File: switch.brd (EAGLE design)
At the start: 11.6 x 31.7 mm, 3 parts

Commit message: updated
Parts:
- U$1: value MICROBIT_PAD -> pin1
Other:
- board size 11.6 x 31.7 mm -> 11.6 x 37.7 mm
- board text added: "PinwheelRobotics"
- board text added: "care@pinwheel"
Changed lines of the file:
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@@
 <setting verticaltext="up"/>
 </settings>
-<grid distance="50" unitdist="mil" unit="mm" style="lines" multiple="1" display="yes" altdistance="5" altunitdist="mil" altunit="mm"/>
+<grid distance="0.5" unitdist="mm" unit="mm" style="lines" multiple="1" display="yes" altdistance="5" altunitdist="mil" altunit="mm"/>
 <layers>
 <layer number="1" name="Top" color="4" fill="1" visible="yes" active="yes"/>
@@
 <layer number="43" name="vRestrict" color="2" fill="10" visible="yes" active="yes"/>
 <layer number="44" name="Drills" color="7" fill="1" visible="no" active="yes"/>
-<layer number="45" name="Holes" color="7" fill="1" visible="no" active="yes"/>
+<layer number="45" name="Holes" color="7" fill="1" visible="yes" active="yes"/>
 <layer number="46" name="Milling" color="3" fill="1" visible="no" active="yes"/>
 <layer number="47" name="Measures" color="7" fill="1" visible="no" active="yes"/>
@@
 <board>
 <plain>
-<wire x1="13.97" y1="11.43" x2="25.578" y2="11.43" width="0" layer="20"/>
-<wire x1="25.578" y1="11.43" x2="25.578" y2="43.17" width="0" layer="20"/>
-<wire x1="25.578" y1="43.17" x2="13.97" y2="43.17" width="0" layer="20"/>
-<wire x1="13.97" y1="43.17" x2="13.97" y2="11.43" width="0" layer="20"/>
+<wire x1="13.97" y1="45.206540625" x2="13.97" y2="10.297284375" width="0" layer="20"/>
+<wire x1="13.97" y1="10.297284375" x2="15.837284375" y2="8.43" width="0" layer="20" curve="90"/>
+<wire x1="15.837284375" y1="8.43" x2="23.637571875" y2="8.43" width="0" layer="20"/>
+<wire x1="23.637571875" y1="8.43" x2="25.578" y2="10.370428125" width="0" layer="20" curve="90"/>
+<wire x1="25.578" y1="10.370428125" x2="25.578" y2="45.098121875" width="0" layer="20"/>
+<wire x1="25.578" y1="45.098121875" x2="24.506121875" y2="46.17" width="0" layer="20" curve="90"/>
+<wire x1="24.506121875" y1="46.17" x2="14.933459375" y2="46.17" width="0" layer="20"/>
+<wire x1="14.933459375" y1="46.17" x2="13.97" y2="45.206540625" width="0" layer="20" curve="90"/>
+<hole x="16.004" y="10.574" drill="3"/>
+<hole x="23.498" y="10.574" drill="3"/>
+<hole x="16.004" y="43.884" drill="3"/>
+<hole x="23.496" y="44.006" drill="3"/>
+<text x="16.121" y="18.613" size="1.4224" layer="21" rot="R90">PinwheelRobotics</text>
+<text x="25.35" y="33.449" size="1.4224" layer="22" rot="MR270">care@pinwheel</text>
 </plain>
 <attributes>
@@
 <attribute name="SF_SKU" value="COM-00097" x="-1.27" y="62.865" size="1.778" layer="27" rot="R180" display="off"/>
 </element>
-<element name="U$1" library="microbit" package="MICROBIT_PAD" value="MICROBIT_PAD" x="20.066" y="15.748" smashed="yes" rot="R180">
-<attribute name="NAME" x="15.24" y="21.59" size="1.27" layer="21" rot="R270"/>
-</element>
-<element name="U$2" library="microbit" package="MICROBIT_PAD" value="MICROBIT_PAD" x="20.193" y="38.862" smashed="yes">
-<attribute name="NAME" x="16.129" y="36.703" size="1.27" layer="21" rot="R90"/>
-</element>
+<element name="U$1" library="microbit" package="MICROBIT_PAD" value="pin1" x="20.066" y="15.748" smashed="yes" rot="R180"/>
+<element name="U$2" library="microbit" package="MICROBIT_PAD" value="MICROBIT_PAD" x="20.193" y="38.862" smashed="yes"/>
 </elements>
 <signals>

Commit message: New Updates
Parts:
- moved U$1 3.82 mm to (19.8, 19.6), turned to 0 degrees
- moved S1 2.71 mm to (19.8, 30.0)
- moved U$2 0.63 mm to (19.8, 39.4), turned to 180 degrees
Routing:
- net N$2: track 13.3 -> 8.48 mm
- net N$1: track 13.2 -> 9.50 mm
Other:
- board size 11.6 x 37.7 mm -> 14.5 x 34 mm
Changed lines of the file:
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@@
 <drawing>
 <settings>
-<setting alwaysvectorfont="yes"/>
+<setting alwaysvectorfont="no"/>
 <setting verticaltext="up"/>
 </settings>
@@
 <board>
 <plain>
-<wire x1="13.97" y1="45.206540625" x2="13.97" y2="10.297284375" width="0" layer="20"/>
-<wire x1="13.97" y1="10.297284375" x2="15.837284375" y2="8.43" width="0" layer="20" curve="90"/>
-<wire x1="15.837284375" y1="8.43" x2="23.637571875" y2="8.43" width="0" layer="20"/>
-<wire x1="23.637571875" y1="8.43" x2="25.578" y2="10.370428125" width="0" layer="20" curve="90"/>
-<wire x1="25.578" y1="10.370428125" x2="25.578" y2="45.098121875" width="0" layer="20"/>
-<wire x1="25.578" y1="45.098121875" x2="24.506121875" y2="46.17" width="0" layer="20" curve="90"/>
-<wire x1="24.506121875" y1="46.17" x2="14.933459375" y2="46.17" width="0" layer="20"/>
-<wire x1="14.933459375" y1="46.17" x2="13.97" y2="45.206540625" width="0" layer="20" curve="90"/>
-<hole x="16.004" y="10.574" drill="3"/>
-<hole x="23.498" y="10.574" drill="3"/>
-<hole x="16.004" y="43.884" drill="3"/>
-<hole x="23.496" y="44.006" drill="3"/>
-<text x="16.121" y="18.613" size="1.4224" layer="21" rot="R90">PinwheelRobotics</text>
-<text x="25.35" y="33.449" size="1.4224" layer="22" rot="MR270">care@pinwheel</text>
+<hole x="14.5" y="14.511" drill="3"/>
+<hole x="25" y="14.5" drill="3"/>
+<hole x="14.5" y="44.5" drill="3"/>
+<hole x="25" y="44.5" drill="3"/>
+<text x="15.232" y="20.772" size="1.4224" layer="21" rot="R90">PinwheelRobotics</text>
+<text x="26.112" y="34.211" size="1.4224" layer="22" rot="MR270">care@pinwheel</text>
+<wire x1="27" y1="13.394378125" x2="27" y2="45.257834375" width="0.1524" layer="20"/>
+<wire x1="27" y1="45.257834375" x2="25.757834375" y2="46.5" width="0.1524" layer="20" curve="90"/>
+<wire x1="25.757834375" y1="46.5" x2="13.9548875" y2="46.5" width="0.1524" layer="20"/>
+<wire x1="13.9548875" y1="46.5" x2="12.5" y2="45.0451125" width="0.1524" layer="20" curve="90"/>
+<wire x1="12.5" y1="45.0451125" x2="12.5" y2="13.58015" width="0.1524" layer="20"/>
+<wire x1="12.5" y1="13.58015" x2="13.58015" y2="12.5" width="0.1524" layer="20" curve="90"/>
+<wire x1="13.58015" y1="12.5" x2="26.105621875" y2="12.5" width="0.1524" layer="20"/>
+<wire x1="26.105621875" y1="12.5" x2="27" y2="13.394378125" width="0.1524" layer="20" curve="90"/>
 </plain>
 <attributes>
@@
 </autorouter>
 <elements>
-<element name="S1" library="SparkFun-Switches" library_urn="urn:adsk.eagle:library:535" package="TACTILE_SWITCH_PTH_6.0MM" package3d_urn="urn:adsk.eagle:package:40163/1" value="MOMENTARY-SWITCH-SPST-PTH-6.0MM" x="20.32" y="27.305" smashed="yes" rot="R180">
-<attribute name="NAME" x="23.876" y="27.051" size="0.6096" layer="25" font="vector" ratio="20" rot="R270" align="bottom-center"/>
-<attribute name="PROD_ID" value=" SWCH-08441" x="-1.27" y="62.865" size="1.778" layer="27" rot="R180" display="off"/>
-<attribute name="SF_SKU" value="COM-00097" x="-1.27" y="62.865" size="1.778" layer="27" rot="R180" display="off"/>
+<element name="S1" library="SparkFun-Switches" library_urn="urn:adsk.eagle:library:535" package="TACTILE_SWITCH_PTH_6.0MM" package3d_urn="urn:adsk.eagle:package:40163/1" value="MOMENTARY-SWITCH-SPST-PTH-6.0MM" x="19.812" y="29.972" smashed="yes" rot="R180">
+<attribute name="NAME" x="23.368" y="29.718" size="0.6096" layer="25" font="vector" ratio="20" rot="R270" align="bottom-center"/>
+<attribute name="PROD_ID" value=" SWCH-08441" x="-1.778" y="65.532" size="1.778" layer="27" rot="R180" display="off"/>
+<attribute name="SF_SKU" value="COM-00097" x="-1.778" y="65.532" size="1.778" layer="27" rot="R180" display="off"/>
 </element>
-<element name="U$1" library="microbit" package="MICROBIT_PAD" value="pin1" x="20.066" y="15.748" smashed="yes" rot="R180"/>
-<element name="U$2" library="microbit" package="MICROBIT_PAD" value="MICROBIT_PAD" x="20.193" y="38.862" smashed="yes"/>
+<element name="U$1" library="microbit" package="MICROBIT_PAD" value="pin1" x="19.812" y="19.558" smashed="yes"/>
+<element name="U$2" library="microbit" package="MICROBIT_PAD" value="MICROBIT_PAD" x="19.812" y="39.37" smashed="yes" rot="R180"/>
 </elements>
 <signals>
@@
 <contactref element="U$1" pad="PAD"/>
 <contactref element="S1" pad="1"/>
-<wire x1="23.622" y1="15.6972" x2="23.622" y2="24.9936" width="0.1524" layer="16"/>
-<wire x1="23.3172" y1="15.3924" x2="23.622" y2="15.6972" width="0.1524" layer="16"/>
-<wire x1="20.4216" y1="15.3924" x2="23.3172" y2="15.3924" width="0.1524" layer="16"/>
-<wire x1="20.066" y1="15.748" x2="20.4216" y2="15.3924" width="0.1524" layer="16"/>
-<wire x1="23.622" y1="24.9936" x2="23.5712" y2="25.0444" width="0.1524" layer="16"/>
+<wire x1="23.0632" y1="27.7114" x2="23.0632" y2="22.8092" width="0.6096" layer="16"/>
+<wire x1="23.0632" y1="22.8092" x2="19.812" y2="19.558" width="0.6096" layer="16"/>
 </signal>
 <signal name="N$2">
 <contactref element="U$2" pad="PAD"/>
 <contactref element="S1" pad="3"/>
-<wire x1="23.622" y1="31.6992" x2="23.622" y2="29.5656" width="0.1524" layer="16"/>
-<wire x1="23.7744" y1="31.8516" x2="23.622" y2="31.6992" width="0.1524" layer="16"/>
-<wire x1="23.7744" y1="39.0144" x2="23.7744" y2="31.8516" width="0.1524" layer="16"/>
-<wire x1="23.622" y1="39.1668" x2="23.7744" y2="39.0144" width="0.1524" layer="16"/>
-<wire x1="20.574" y1="39.1668" x2="23.622" y2="39.1668" width="0.1524" layer="16"/>
-<wire x1="20.2692" y1="38.862" x2="20.574" y2="39.1668" width="0.1524" layer="16"/>
-<wire x1="23.622" y1="29.5656" x2="23.5712" y2="29.5656" width="0.1524" layer="16"/>
-<wire x1="20.2692" y1="38.862" x2="20.193" y2="38.862" width="0.1524" layer="16"/>
+<wire x1="23.0632" y1="32.2326" x2="23.0632" y2="36.1188" width="0.6096" layer="16"/>
+<wire x1="23.0632" y1="36.1188" x2="19.812" y2="39.37" width="0.6096" layer="16"/>
 </signal>
 </signals>

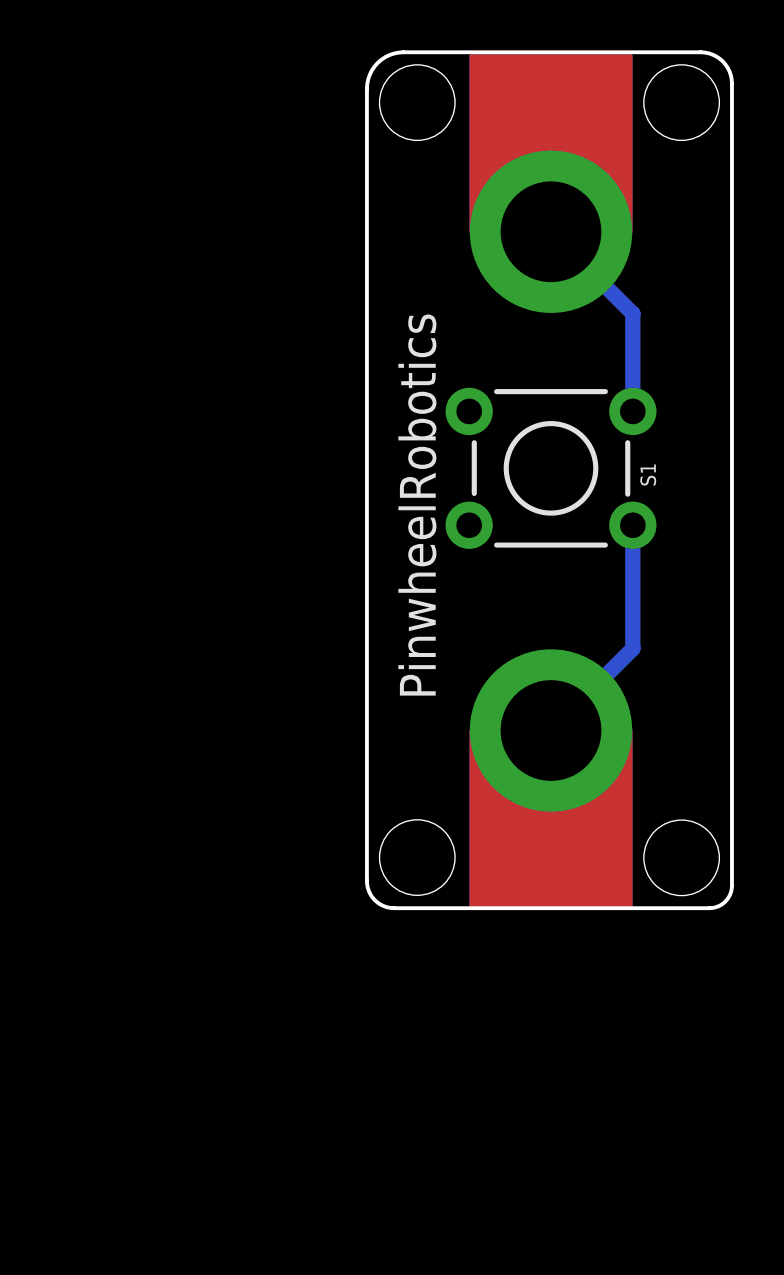
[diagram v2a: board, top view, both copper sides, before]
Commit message: New Update for board curv
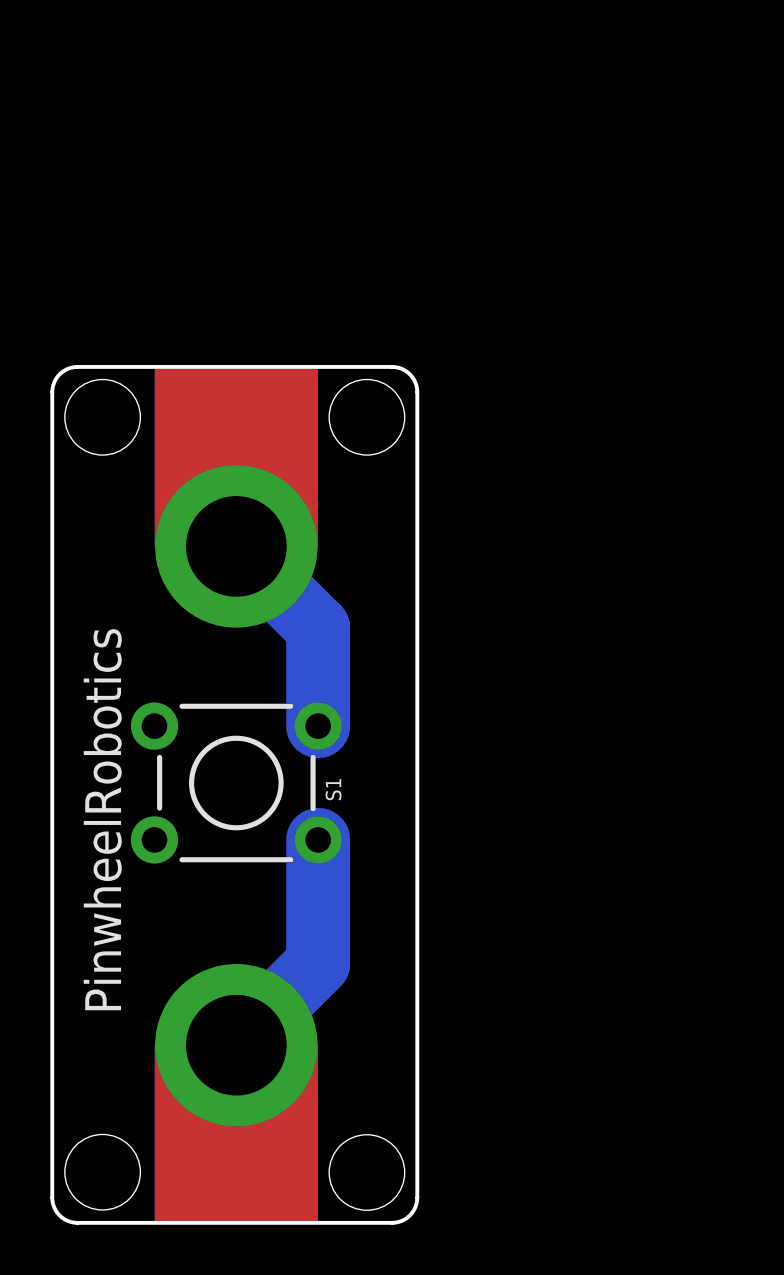
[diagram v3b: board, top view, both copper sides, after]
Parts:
- moved S1 17.7 mm to (7.31, 17.5)
- moved U$1 17.7 mm to (7.31, 7.06)
- moved U$2 17.7 mm to (7.31, 26.9)
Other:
- outline, holes or cut-outs redrawn
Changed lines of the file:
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@@
 <drawing>
 <settings>
-<setting alwaysvectorfont="no"/>
+<setting alwaysvectorfont="yes"/>
 <setting verticaltext="up"/>
 </settings>
@@
 <board>
 <plain>
-<hole x="14.5" y="14.511" drill="3"/>
-<hole x="25" y="14.5" drill="3"/>
-<hole x="14.5" y="44.5" drill="3"/>
-<hole x="25" y="44.5" drill="3"/>
-<text x="15.232" y="20.772" size="1.4224" layer="21" rot="R90">PinwheelRobotics</text>
-<text x="26.112" y="34.211" size="1.4224" layer="22" rot="MR270">care@pinwheel</text>
-<wire x1="27" y1="13.394378125" x2="27" y2="45.257834375" width="0.1524" layer="20"/>
-<wire x1="27" y1="45.257834375" x2="25.757834375" y2="46.5" width="0.1524" layer="20" curve="90"/>
-<wire x1="25.757834375" y1="46.5" x2="13.9548875" y2="46.5" width="0.1524" layer="20"/>
-<wire x1="13.9548875" y1="46.5" x2="12.5" y2="45.0451125" width="0.1524" layer="20" curve="90"/>
-<wire x1="12.5" y1="45.0451125" x2="12.5" y2="13.58015" width="0.1524" layer="20"/>
-<wire x1="12.5" y1="13.58015" x2="13.58015" y2="12.5" width="0.1524" layer="20" curve="90"/>
-<wire x1="13.58015" y1="12.5" x2="26.105621875" y2="12.5" width="0.1524" layer="20"/>
-<wire x1="26.105621875" y1="12.5" x2="27" y2="13.394378125" width="0.1524" layer="20" curve="90"/>
+<hole x="2" y="2.011" drill="3"/>
+<hole x="12.5" y="2" drill="3"/>
+<hole x="2" y="32" drill="3"/>
+<hole x="12.5" y="32" drill="3"/>
+<text x="2.732" y="8.272" size="1.4224" layer="21" rot="R90">PinwheelRobotics</text>
+<text x="13.612" y="21.711" size="1.4224" layer="22" rot="MR270">care@pinwheel</text>
+<wire x1="0" y1="33" x2="0" y2="1" width="0.1524" layer="20"/>
+<wire x1="0" y1="1" x2="1" y2="0" width="0.1524" layer="20" curve="90"/>
+<wire x1="1" y1="0" x2="13.5" y2="0" width="0.1524" layer="20"/>
+<wire x1="13.5" y1="0" x2="14.5" y2="1" width="0.1524" layer="20" curve="90"/>
+<wire x1="14.5" y1="1" x2="14.5" y2="33" width="0.1524" layer="20"/>
+<wire x1="14.5" y1="33" x2="13.5" y2="34" width="0.1524" layer="20" curve="90"/>
+<wire x1="13.5" y1="34" x2="1" y2="34" width="0.1524" layer="20"/>
+<wire x1="1" y1="34" x2="0" y2="33" width="0.1524" layer="20" curve="90"/>
 </plain>
 <attributes>
@@
 </autorouter>
 <elements>
-<element name="S1" library="SparkFun-Switches" library_urn="urn:adsk.eagle:library:535" package="TACTILE_SWITCH_PTH_6.0MM" package3d_urn="urn:adsk.eagle:package:40163/1" value="MOMENTARY-SWITCH-SPST-PTH-6.0MM" x="19.812" y="29.972" smashed="yes" rot="R180">
-<attribute name="NAME" x="23.368" y="29.718" size="0.6096" layer="25" font="vector" ratio="20" rot="R270" align="bottom-center"/>
-<attribute name="PROD_ID" value=" SWCH-08441" x="-1.778" y="65.532" size="1.778" layer="27" rot="R180" display="off"/>
-<attribute name="SF_SKU" value="COM-00097" x="-1.778" y="65.532" size="1.778" layer="27" rot="R180" display="off"/>
+<element name="S1" library="SparkFun-Switches" library_urn="urn:adsk.eagle:library:535" package="TACTILE_SWITCH_PTH_6.0MM" package3d_urn="urn:adsk.eagle:package:40163/1" value="MOMENTARY-SWITCH-SPST-PTH-6.0MM" x="7.312" y="17.472" smashed="yes" rot="R180">
+<attribute name="NAME" x="10.868" y="17.218" size="0.6096" layer="25" font="vector" ratio="20" rot="R270" align="bottom-center"/>
+<attribute name="PROD_ID" value=" SWCH-08441" x="-14.278" y="53.032" size="1.778" layer="27" rot="R180" display="off"/>
+<attribute name="SF_SKU" value="COM-00097" x="-14.278" y="53.032" size="1.778" layer="27" rot="R180" display="off"/>
 </element>
-<element name="U$1" library="microbit" package="MICROBIT_PAD" value="pin1" x="19.812" y="19.558" smashed="yes"/>
-<element name="U$2" library="microbit" package="MICROBIT_PAD" value="MICROBIT_PAD" x="19.812" y="39.37" smashed="yes" rot="R180"/>
+<element name="U$1" library="microbit" package="MICROBIT_PAD" value="pin1" x="7.312" y="7.058" smashed="yes"/>
+<element name="U$2" library="microbit" package="MICROBIT_PAD" value="MICROBIT_PAD" x="7.312" y="26.87" smashed="yes" rot="R180"/>
 </elements>
 <signals>
@@
 <contactref element="U$1" pad="PAD"/>
 <contactref element="S1" pad="1"/>
-<wire x1="23.0632" y1="27.7114" x2="23.0632" y2="22.8092" width="0.6096" layer="16"/>
-<wire x1="23.0632" y1="22.8092" x2="19.812" y2="19.558" width="0.6096" layer="16"/>
+<wire x1="10.5632" y1="15.2114" x2="10.5632" y2="10.3092" width="2.54" layer="16"/>
+<wire x1="10.5632" y1="10.3092" x2="7.312" y2="7.058" width="2.54" layer="16"/>
 </signal>
 <signal name="N$2">
 <contactref element="U$2" pad="PAD"/>
 <contactref element="S1" pad="3"/>
-<wire x1="23.0632" y1="32.2326" x2="23.0632" y2="36.1188" width="0.6096" layer="16"/>
-<wire x1="23.0632" y1="36.1188" x2="19.812" y2="39.37" width="0.6096" layer="16"/>
+<wire x1="10.5632" y1="19.7326" x2="10.5632" y2="23.6188" width="2.54" layer="16"/>
+<wire x1="10.5632" y1="23.6188" x2="7.312" y2="26.87" width="2.54" layer="16"/>
 </signal>
 </signals>
